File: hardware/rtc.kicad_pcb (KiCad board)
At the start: 2 copper layers, 25 x 25 mm, 16 parts, among them P1 CON-SENSOR, U1 M24C64, U2 PCF85263AT, U3 DRILL, U4 DRILL, U5 DRILL, U6 DRILL, X1 32.768kHz

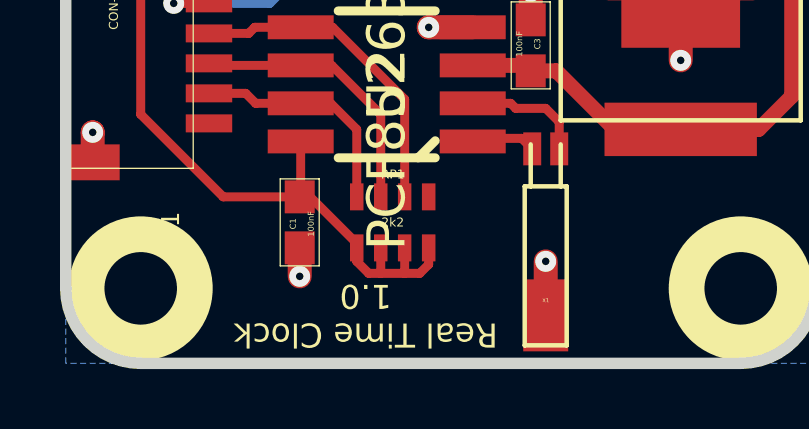
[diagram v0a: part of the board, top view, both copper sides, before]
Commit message: change rtc battery footprint
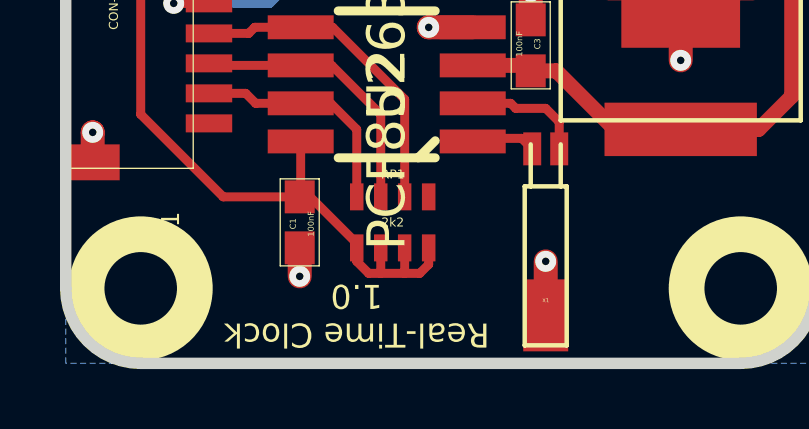
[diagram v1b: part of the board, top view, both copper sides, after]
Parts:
- moved VAL 0.40 mm to (143.7, 100.6), turned to 0 degrees
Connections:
- P1 pad 1: (no net) -> Net-(P1-Pad1)
- P1 pad 10: (no net) -> Net-(P1-Pad10)
- RP1 pad 4: (no net) -> Net-(RP1-Pad4)
- U1 pad 7: (no net) -> Net-(U1-Pad7)
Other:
- board text added: "Real-Time Clock 1.0"
- board text removed: "Real Time Clock 1.0"
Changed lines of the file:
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@@
-(kicad_pcb (version 4) (host pcbnew "(2015-03-18 BZR 5525)-product")
+(kicad_pcb (version 4) (host pcbnew 4.0.1-3.201512221401+6198~38~ubuntu15.10.1-stable)
   (general
     (links 33)
     (no_connects 0)
-    (area 124.445139 87.245139 282.895869 162.490743)
+    (area 125.109499 87.909499 150.490501 113.290501)
     (thickness 1.6002)
     (drawings 11)
@@
     (zones 0)
     (modules 16)
-    (nets 12)
+    (nets 16)
   )
   (page A4)
@@
     (visible_elements FFFFFF9F)
     (pcbplotparams
-      (layerselection 0x00030_80000001)
+      (layerselection 0x010f8_80000001)
       (usegerberextensions true)
       (excludeedgelayer true)
@@
       (drillshape 0)
       (scaleselection 1)
-      (outputdirectory prod/))
+      (outputdirectory best/))
   )
   (net 0 "")
@@
   (net 10 3V3)
   (net 11 "Net-(BT1-Pad1)")
+  (net 12 "Net-(P1-Pad1)")
+  (net 13 "Net-(P1-Pad10)")
+  (net 14 "Net-(RP1-Pad4)")
+  (net 15 "Net-(U1-Pad7)")
   (net_class Default "Dies ist die voreingestellte Netzklasse."
     (clearance 0.14986)
@@
     (add_net GND)
     (add_net "Net-(BT1-Pad1)")
+    (add_net "Net-(P1-Pad1)")
+    (add_net "Net-(P1-Pad10)")
     (add_net "Net-(P1-Pad6)")
     (add_net "Net-(P1-Pad7)")
     (add_net "Net-(P1-Pad8)")
     (add_net "Net-(P1-Pad9)")
+    (add_net "Net-(RP1-Pad4)")
+    (add_net "Net-(U1-Pad7)")
     (add_net "Net-(U2-Pad1)")
     (add_net "Net-(U2-Pad2)")
@@
   (module kicad-libraries:CON-SENSOR (layer Vorderseite)
     (at 125.3 100.6 270)
+    (attr smd)
     (fp_text reference P1 (at 7.9502 -3.50012 270) (layer F.SilkS)
       (effects (font (size 0.59944 0.59944) (thickness 0.12446)))
@@
     (fp_line (start -5.99948 -4.24942) (end -5.99948 0) (layer F.SilkS) (width 0.01))
     (fp_line (start -5.99948 0) (end 5.99948 0) (layer F.SilkS) (width 0.01))
-    (pad 1 smd rect (at -4.50088 -4.7752 270) (size 0.59944 1.5494) (layers Vorderseite F.Paste F.Mask))
+    (pad 1 smd rect (at -4.50088 -4.7752 270) (size 0.59944 1.5494) (layers Vorderseite F.Paste F.Mask)
+      (net 12 "Net-(P1-Pad1)"))
     (pad 2 smd rect (at -3.50012 -4.7752 270) (size 0.59944 1.5494) (layers Vorderseite F.Paste F.Mask)
       (net 1 GND))
@@
     (pad 9 smd rect (at 3.50012 -4.7752 270) (size 0.59944 1.5494) (layers Vorderseite F.Paste F.Mask)
       (net 7 "Net-(P1-Pad9)"))
-    (pad 10 smd rect (at 4.50088 -4.7752 270) (size 0.59944 1.5494) (layers Vorderseite F.Paste F.Mask))
+    (pad 10 smd rect (at 4.50088 -4.7752 270) (size 0.59944 1.5494) (layers Vorderseite F.Paste F.Mask)
+      (net 13 "Net-(P1-Pad10)"))
     (pad EP smd rect (at -5.79882 -0.89916 270) (size 1.19888 1.80086) (layers Vorderseite F.Paste F.Mask)
       (net 1 GND))
@@
   (module kicad-libraries:SOIC8 (layer Vorderseite)
     (at 136 96.6 270)
+    (attr smd)
     (fp_text reference U1 (at 3.29946 2.60096 270) (layer F.SilkS)
       (effects (font (size 0.29972 0.29972) (thickness 0.0762)))
@@
     (pad 6 smd rect (at 0.63246 -2.69748 270) (size 0.59944 1.5494) (layers Vorderseite F.Paste F.Mask)
       (net 2 SCL))
-    (pad 7 smd rect (at -0.63246 -2.69748 270) (size 0.59944 1.5494) (layers Vorderseite F.Paste F.Mask))
+    (pad 7 smd rect (at -0.63246 -2.69748 270) (size 0.59944 1.5494) (layers Vorderseite F.Paste F.Mask)
+      (net 15 "Net-(U1-Pad7)"))
     (pad 8 smd rect (at -1.90246 -2.69748 270) (size 0.59944 1.5494) (layers Vorderseite F.Paste F.Mask)
       (net 10 3V3))
@@
   (module kicad-libraries:4X0603 (layer Vorderseite)
     (at 136.2 108.4)
+    (attr smd)
     (fp_text reference RP1 (at 0 -1.6002) (layer F.SilkS)
       (effects (font (size 0.29972 0.29972) (thickness 0.0762)))
@@
     (pad 3 smd rect (at 0.39878 -0.8509) (size 0.44958 0.89916) (layers Vorderseite F.Paste F.Mask)
       (net 5 "Net-(P1-Pad7)"))
-    (pad 4 smd rect (at 1.19888 -0.8509) (size 0.44958 0.89916) (layers Vorderseite F.Paste F.Mask))
+    (pad 4 smd rect (at 1.19888 -0.8509) (size 0.44958 0.89916) (layers Vorderseite F.Paste F.Mask)
+      (net 14 "Net-(RP1-Pad4)"))
     (pad 5 smd rect (at 1.19888 0.8509) (size 0.44958 0.89916) (layers Vorderseite F.Paste F.Mask)
       (net 10 3V3))
@@
   (module kicad-libraries:SO-8 (layer Vorderseite)
     (at 136 103.8 90)
+    (attr smd)
     (fp_text reference U2 (at 0 0 90) (layer F.SilkS)
       (effects (font (thickness 0.3048)))
@@
   (module kicad-libraries:AB26TRQ (layer Vorderseite)
     (at 141.3 111.5 180)
+    (attr smd)
     (fp_text reference X1 (at 0 0.5 180) (layer F.SilkS)
       (effects (font (size 0.127 0.127) (thickness 0.03175)))
@@
       (net 8 "Net-(U2-Pad1)"))
   )
-  (module kicad-libraries:BATTERY_HOLDER_2998 (layer Vorderseite)
-    (at 145.8 100.6 90)
-    (fp_text reference BT1 (at 0 0.5 90) (layer F.SilkS)
-      (effects (font (size 0.15 0.15) (thickness 0.0375)))
-    )
-    (fp_text value BATTERY (at 0 -0.5 90) (layer F.Fab)
-      (effects (font (size 0.15 0.15) (thickness 0.0375)))
-    )
-    (fp_line (start -4.4 -4) (end 4.4 -4) (layer F.SilkS) (width 0.15))
-    (fp_line (start 4.4 -4) (end 4.4 4) (layer F.SilkS) (width 0.15))
-    (fp_line (start 4.4 4) (end -4.4 4) (layer F.SilkS) (width 0.15))
-    (fp_line (start -4.4 4) (end -4.4 -4) (layer F.SilkS) (width 0.15))
-    (pad 1 smd rect (at -4.7 0 90) (size 1.78 5.08) (layers Vorderseite F.Paste F.Mask)
-      (net 11 "Net-(BT1-Pad1)"))
-    (pad 1 smd rect (at 4.7 0 90) (size 1.78 5.08) (layers Vorderseite F.Paste F.Mask)
-      (net 11 "Net-(BT1-Pad1)"))
-    (pad 2 smd rect (at 0 0 90) (size 3.96 3.96) (layers Vorderseite F.Paste F.Mask)
-      (net 1 GND))
-  )
   (module kicad-libraries:Logo_31x31 (layer Vorderseite)
     (at 143.2 93.8 180)
+    (attr smd)
     (fp_text reference G*** (at 1.34874 2.97434 180) (layer F.SilkS) hide
       (effects (font (size 0.29972 0.29972) (thickness 0.0762)))
@@
   (module kicad-libraries:WEEE_7mm_back (layer Rückseite)
     (at 132.8 100.6 180)
+    (attr smd)
     (fp_text reference VAL (at 0 0 180) (layer B.SilkS) hide
       (effects (font (size 1.143 1.143) (thickness 0.1778)) (justify mirror))
@@
   )
   (module kicad-libraries:CE_5mm (layer Rückseite)
-    (at 143.3 100.6 180)
-    (fp_text reference VAL (at 0 0 180) (layer B.SilkS) hide
+    (at 143.7 100.6)
+    (attr smd)
+    (fp_text reference VAL (at 0 0) (layer B.SilkS) hide
       (effects (font (size 1.143 1.143) (thickness 0.1778)) (justify mirror))
     )
-    (fp_text value CE_5mm (at 0 0 180) (layer B.SilkS) hide
+    (fp_text value CE_5mm (at 0 0) (layer B.SilkS) hide
       (effects (font (size 1.143 1.143) (thickness 0.1778)) (justify mirror))
     )
@@
       (xy 2.3114 -1.41732) (xy 2.3114 -1.67132) (xy 2.3114 -1.67132)) (layer B.SilkS) (width 0.00254))
   )
+  (module kicad-libraries:BATTERY_HOLDER_2998 (layer Vorderseite)
+    (at 145.8 100.6 90)
+    (attr smd)
+    (fp_text reference BT1 (at 0 0.5 90) (layer F.SilkS)
+      (effects (font (size 0.15 0.15) (thickness 0.0375)))
+    )
+    (fp_text value BATTERY (at 0 -0.5 90) (layer F.Fab)
+      (effects (font (size 0.15 0.15) (thickness 0.0375)))
+    )
+    (fp_line (start -4.4 -4) (end 4.4 -4) (layer F.SilkS) (width 0.15))
+    (fp_line (start 4.4 -4) (end 4.4 4) (layer F.SilkS) (width 0.15))
+    (fp_line (start 4.4 4) (end -4.4 4) (layer F.SilkS) (width 0.15))
+    (fp_line (start -4.4 4) (end -4.4 -4) (layer F.SilkS) (width 0.15))
+    (pad 1 smd rect (at -4.7 0 90) (size 1.78 5.08) (layers Vorderseite F.Paste F.Mask)
+      (net 11 "Net-(BT1-Pad1)"))
+    (pad 1 smd rect (at 4.7 0 90) (size 1.78 5.08) (layers Vorderseite F.Paste F.Mask)
+      (net 11 "Net-(BT1-Pad1)"))
+    (pad 2 smd rect (at 0 0 90) (size 3.96 3.96) (layers Vorderseite F.Mask)
+      (net 1 GND))
+  )
   (gr_line (start 150.3 110.6) (end 150.3 90.6) (angle 90) (layer Edge.Cuts) (width 0.381))
   (gr_line (start 127.8 113.1) (end 147.8 113.1) (angle 90) (layer Edge.Cuts) (width 0.381))
@@
     (effects (font (size 0.8001 0.8001) (thickness 0.14986)))
   )
-  (gr_text "Real Time Clock\n1.0" (at 135.3 111.5 180) (layer F.SilkS)
+  (gr_text "Real-Time Clock\n1.0" (at 135 111.5 180) (layer F.SilkS)
     (effects (font (size 0.8001 0.8001) (thickness 0.14986)))
   )

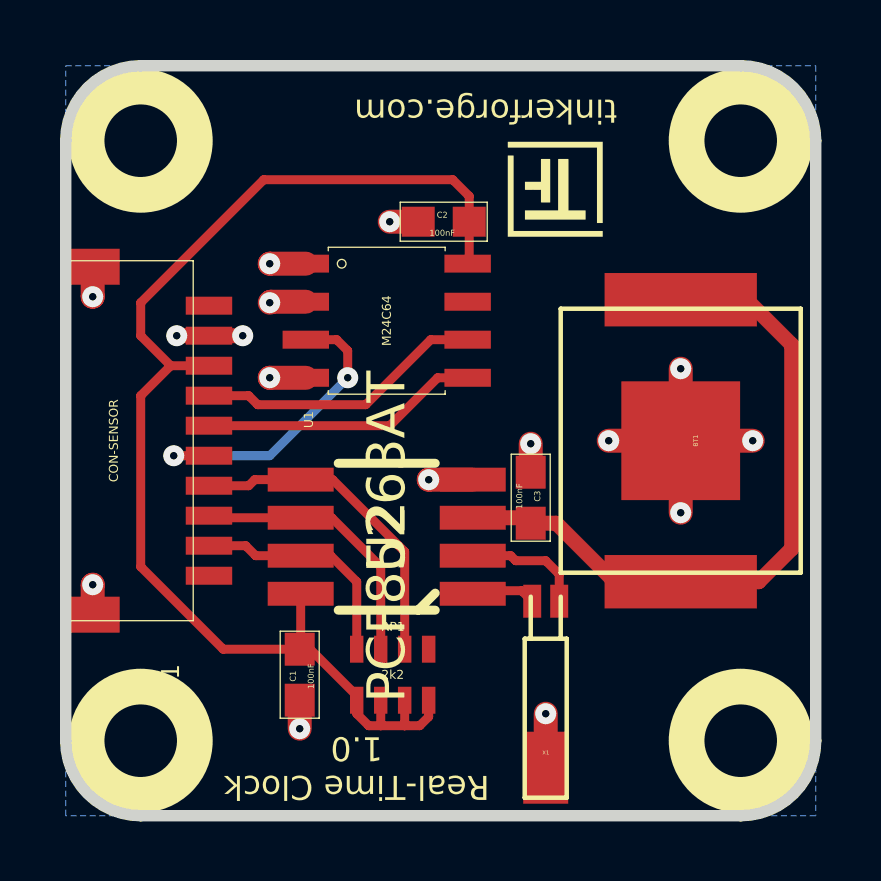
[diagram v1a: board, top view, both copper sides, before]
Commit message: add fiducials
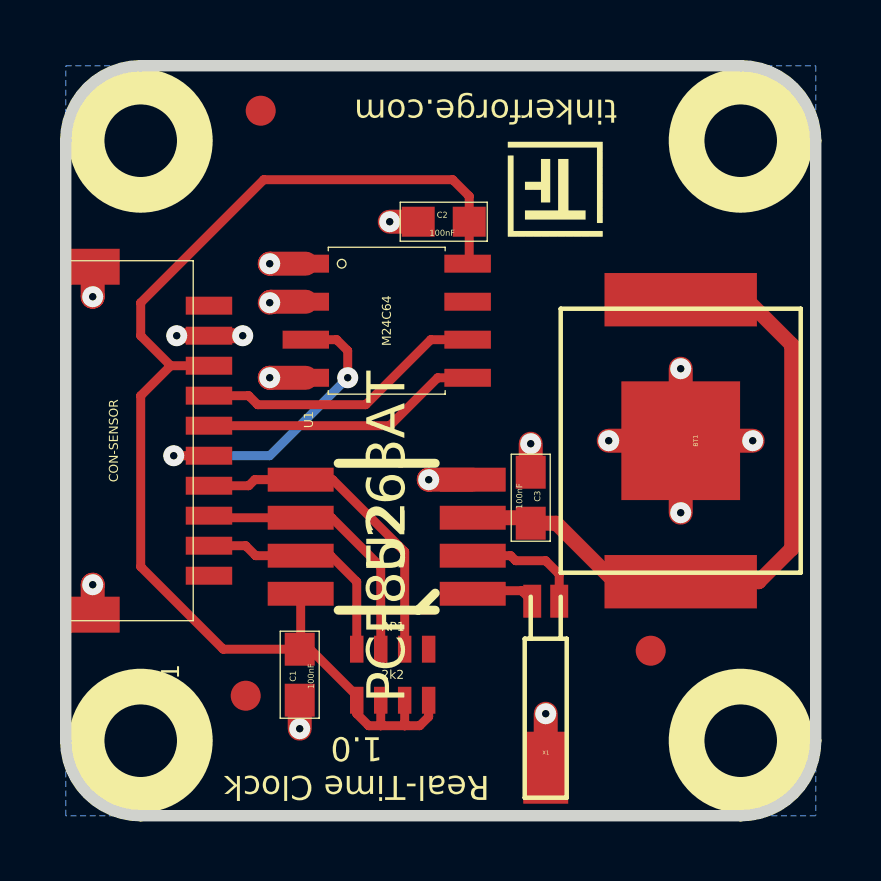
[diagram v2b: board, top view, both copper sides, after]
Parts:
- added Fiducial_Mark: VAL**, kicad-libraries:Fiducial_Mark, F.Cu at (144.8, 107.6)
- added Fiducial_Mark: VAL**, kicad-libraries:Fiducial_Mark, F.Cu at (131.8, 89.6)
- added Fiducial_Mark: VAL**, kicad-libraries:Fiducial_Mark, F.Cu at (131.3, 109.1)
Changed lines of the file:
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@@
     (links 33)
     (no_connects 0)
-    (area 125.109499 87.909499 150.490501 113.290501)
+    (area 124.445139 87.245139 282.895869 162.490743)
     (thickness 1.6002)
     (drawings 11)
     (tracks 123)
     (zones 0)
-    (modules 16)
+    (modules 19)
     (nets 16)
   )
@@
     (visible_elements FFFFFF9F)
     (pcbplotparams
-      (layerselection 0x010f8_80000001)
+      (layerselection 0x010c8_00000001)
       (usegerberextensions true)
       (excludeedgelayer true)
@@
       (drillshape 0)
       (scaleselection 1)
-      (outputdirectory best/))
+      (outputdirectory prod/))
   )
   (net 0 "")
@@
       (net 1 GND))
   )
+  (module kicad-libraries:Fiducial_Mark (layer Vorderseite)
+    (at 144.8 107.6)
+    (attr smd)
+    (fp_text reference Fiducial_Mark (at 0 0) (layer F.SilkS) hide
+      (effects (font (size 0.127 0.127) (thickness 0.03302)))
+    )
+    (fp_text value VAL** (at 0 -0.29972) (layer F.SilkS) hide
+      (effects (font (size 0.127 0.127) (thickness 0.03302)))
+    )
+    (fp_circle (center 0 0) (end 1.15062 0) (layer Dwgs.User) (width 0.01016))
+    (pad 1 smd circle (at 0 0) (size 1.00076 1.00076) (layers Vorderseite F.Paste F.Mask)
+      (clearance 0.65024))
+  )
+  (module kicad-libraries:Fiducial_Mark (layer Vorderseite)
+    (at 131.8 89.6)
+    (attr smd)
+    (fp_text reference Fiducial_Mark (at 0 0) (layer F.SilkS) hide
+      (effects (font (size 0.127 0.127) (thickness 0.03302)))
+    )
+    (fp_text value VAL** (at 0 -0.29972) (layer F.SilkS) hide
+      (effects (font (size 0.127 0.127) (thickness 0.03302)))
+    )
+    (fp_circle (center 0 0) (end 1.15062 0) (layer Dwgs.User) (width 0.01016))
+    (pad 1 smd circle (at 0 0) (size 1.00076 1.00076) (layers Vorderseite F.Paste F.Mask)
+      (clearance 0.65024))
+  )
+  (module kicad-libraries:Fiducial_Mark (layer Vorderseite)
+    (at 131.3 109.1)
+    (attr smd)
+    (fp_text reference Fiducial_Mark (at 0 0) (layer F.SilkS) hide
+      (effects (font (size 0.127 0.127) (thickness 0.03302)))
+    )
+    (fp_text value VAL** (at 0 -0.29972) (layer F.SilkS) hide
+      (effects (font (size 0.127 0.127) (thickness 0.03302)))
+    )
+    (fp_circle (center 0 0) (end 1.15062 0) (layer Dwgs.User) (width 0.01016))
+    (pad 1 smd circle (at 0 0) (size 1.00076 1.00076) (layers Vorderseite F.Paste F.Mask)
+      (clearance 0.65024))
+  )
   (gr_line (start 150.3 110.6) (end 150.3 90.6) (angle 90) (layer Edge.Cuts) (width 0.381))

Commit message: Add 3d information (tbc)
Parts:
- C1, C2, C3: footprint kicad-libraries:0603E -> kicad-libraries:C0603E
